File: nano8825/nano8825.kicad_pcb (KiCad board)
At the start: 2 copper layers, 75 x 90 mm, 24 parts, among them J1 Conn_01x02, J2 Conn_01x04, J3 Conn_01x04, J4 Conn_01x04, J5 Conn_01x02, J6 Conn_01x02, J7 Conn_01x02, J8 Conn_01x02_Female, SW1 SW_DIP_x03, SW2 SW_DIP_x03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

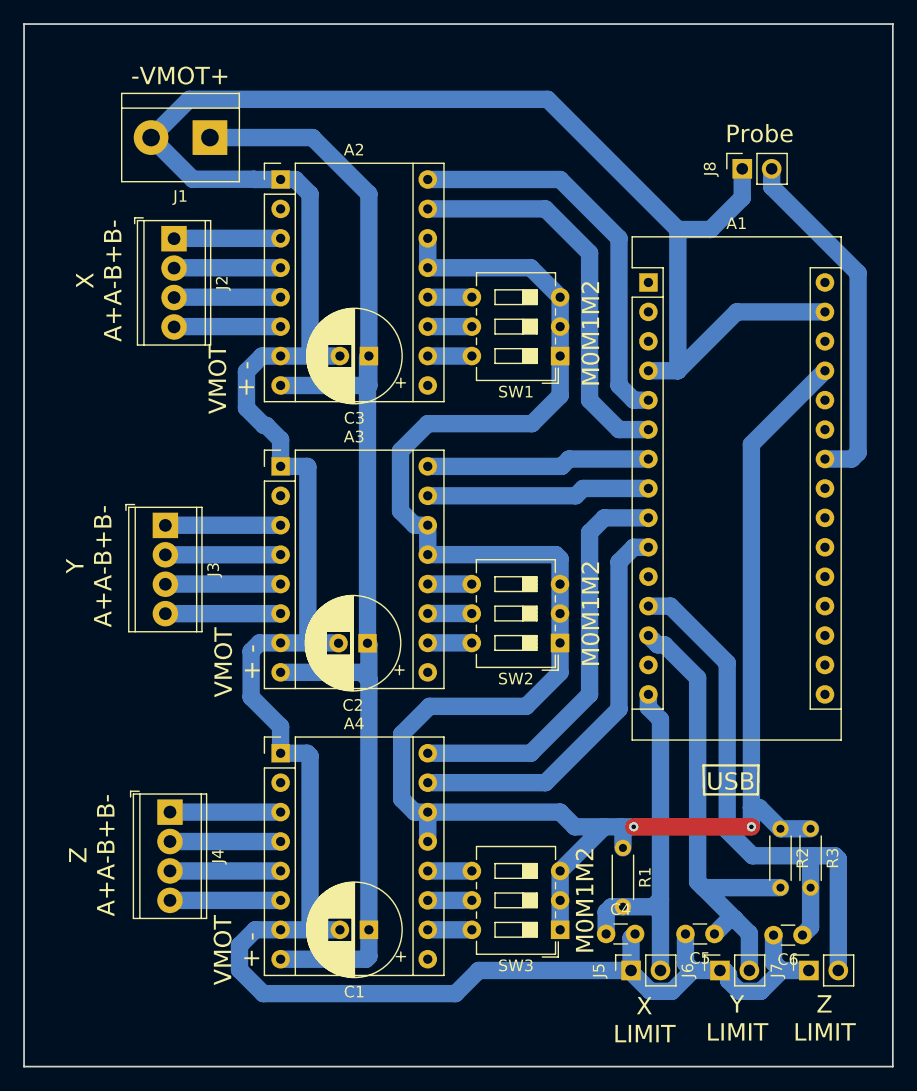
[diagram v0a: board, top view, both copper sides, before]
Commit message: Added Caliper and updated drv8825 board
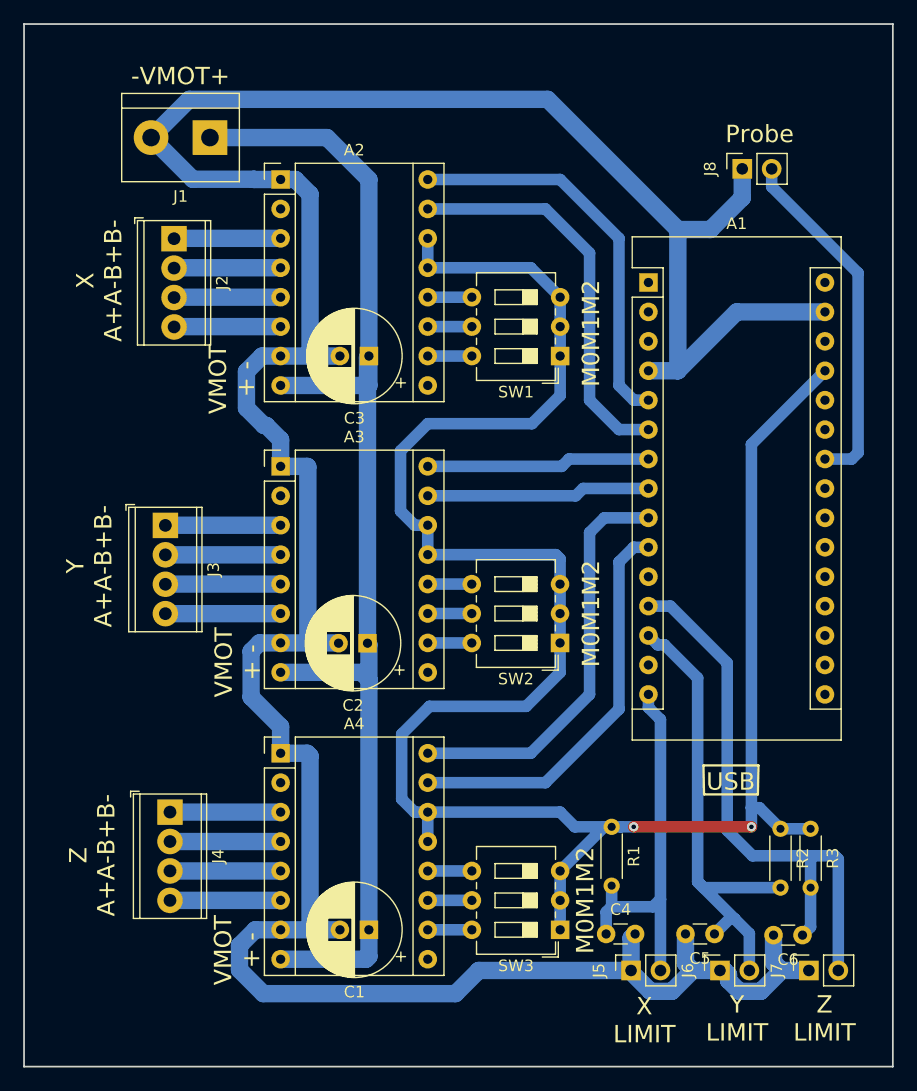
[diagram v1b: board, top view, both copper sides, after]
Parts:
- moved R1 2.06 mm to (160.7, 121.9)
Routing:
- net Net-(A1-Pad27): track 186.7 -> 184.8 mm
- net Net-(A1-Pad15): track 31.3 -> 33.1 mm
- net Net-(A2-Pad8): track 107.4 -> 108.2 mm
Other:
- net class Default: trace_width 1.5 -> 1
- net class StepperPower added: clearance 0.2, trace_width 1.5, via_dia 0.8, via_drill 0.4

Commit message: Updated Layout
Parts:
- moved J7 75.6 mm to (159.4, 61.0)
- moved J5 74.8 mm to (177.2, 61.0)
- moved J6 73.4 mm to (168.3, 61.0)
- moved C4 68.0 mm to (179.7, 66.0), turned to 180 degrees
- moved C6 67.0 mm to (161.9, 66.0)
- moved C5 65.1 mm to (170.8, 66.0)
- moved R3 53.1 mm to (168.1, 69.8), turned to 0 degrees
- moved R2 49.2 mm to (168.1, 73.4), turned to 0 degrees
- moved R1 45.3 mm to (168.1, 77.2), turned to 0 degrees
- moved A1 20.4 mm to (165.1, 95.2)
- moved J8 16.2 mm to (179.7, 79.4), turned to 0 degrees
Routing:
- net Net-(A1-Pad15): track 33.1 -> 77.9 mm
- net Net-(A1-Pad13): track 42.5 -> 75.9 mm
- net Net-(A1-Pad27): track 184.8 -> 209.0 mm, vias 2 -> 0
- net Net-(A1-Pad12): track 50.7 -> 74.0 mm
- net Net-(A1-Pad6): track 34.4 -> 55.2 mm
- net Net-(A1-Pad5): track 34.4 -> 53.7 mm
- net Net-(A1-Pad8): track 19.3 -> 37.4 mm
- net Net-(A1-Pad7): track 19.3 -> 37.4 mm
- net Net-(A1-Pad9): track 35.7 -> 20.3 mm
- net Net-(A1-Pad10): track 34.9 -> 20.3 mm
- net Net-(A1-Pad29): track 266.6 -> 275.6 mm, vias 0 -> 2
- net Net-(A1-Pad24): track 30.7 -> 31.6 mm

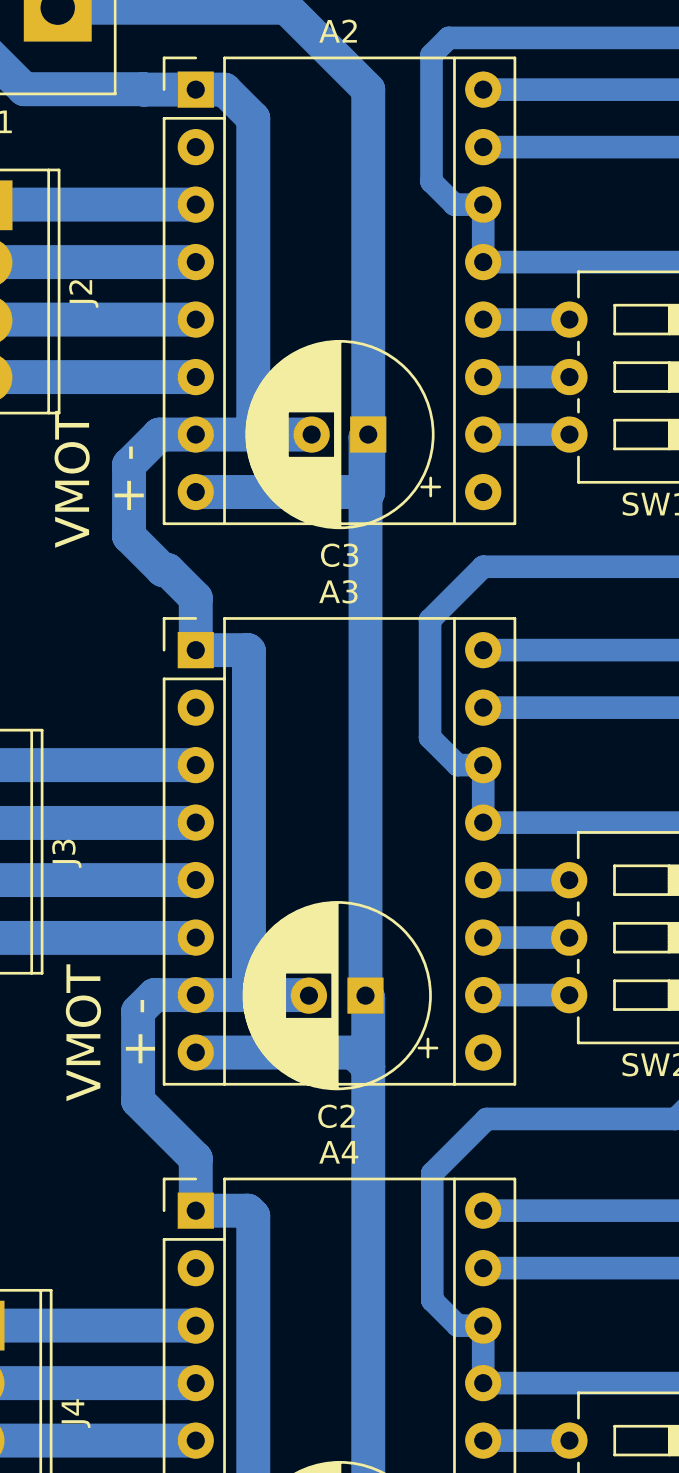
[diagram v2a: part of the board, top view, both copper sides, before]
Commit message: Added FAULT line to force fast decay
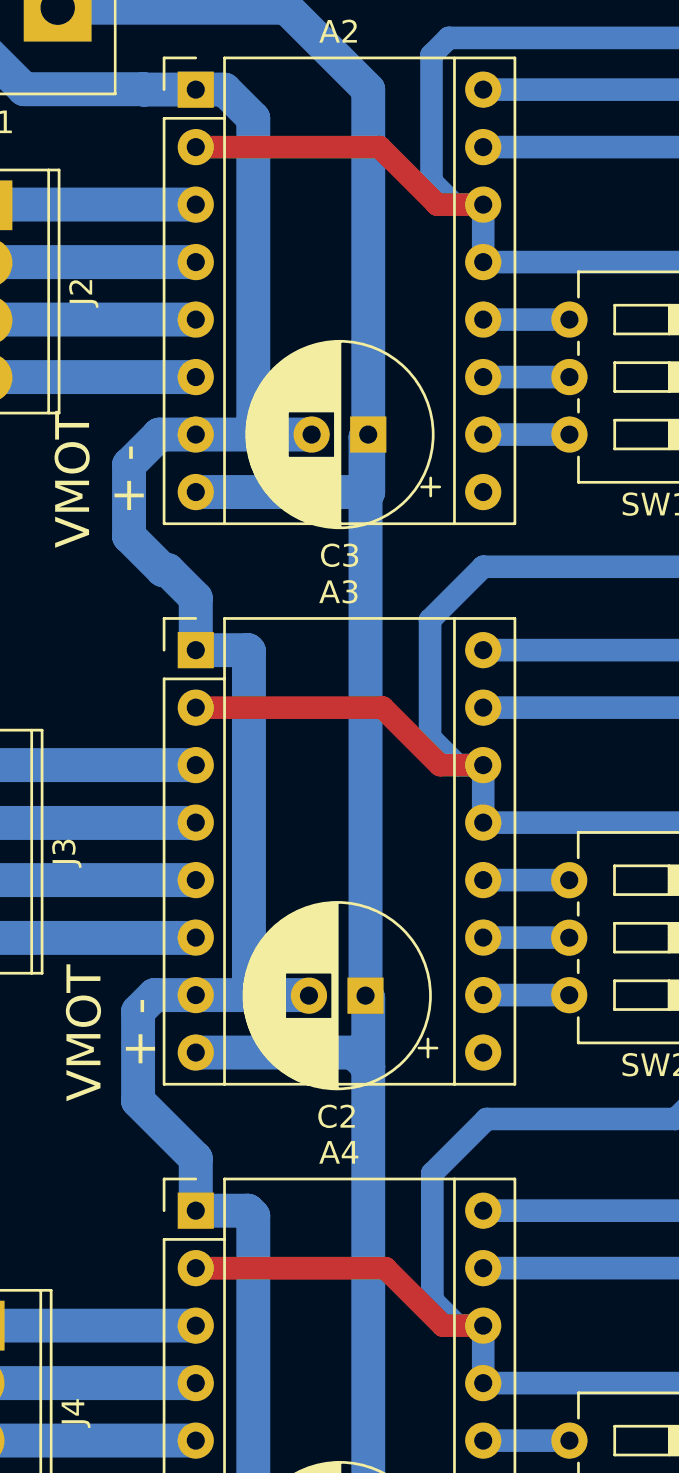
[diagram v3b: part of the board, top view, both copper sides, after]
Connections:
- A2 pad 2: Net-(A2-Pad2) -> Net-(A1-Pad27)
- A3 pad 2: Net-(A3-Pad2) -> Net-(A1-Pad27)
- A4 pad 2: Net-(A4-Pad2) -> Net-(A1-Pad27)
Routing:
- net Net-(A1-Pad27): track 209.0 -> 250.3 mm
